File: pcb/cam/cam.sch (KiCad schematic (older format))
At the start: 93 parts, among them J1 Power In, J2 CONN_PRG_ESP, J3 CONN_PRG_STM, J4 Conn_01x26_Male, J5 SIM_Card, J6 Conn_Coaxial, Q1 IRLML6401, Q2 IRLML6401, U1 ESP32-WROOM-32U, U10 SRV05-4, U11 SIM800C, U2 TPS7A24, U3 FDC610, U4 XC6206-12, U5 XC6206-28, U6 MP2307, U7 MP2307, U8 STM8L051F3P, U9 LY68L6400, Y1 LSE

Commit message: Deleted old pcb; renamed discrete esp-s2 pcb to pcb
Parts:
- removed C22: 1u, Capacitor_SMD:C_0805_2012Metric, symbol Device:C_Small
- removed C24: 22u, 10V, Capacitor_SMD:C_1206_3216Metric, symbol Device:C_Small
- removed C26, C27: 470u, 10V, symbol Device:CP1_Small
- removed C30: 20p, Capacitor_SMD:C_0603_1608Metric, symbol Device:C_Small
- removed C6: 2.2uF, Capacitor_SMD:C_0805_2012Metric, symbol Device:C_Small
- removed J2: CONN_PRG_ESP, symbol Connector:Conn_01x03_Male
- removed J3: CONN_PRG_STM, symbol Connector:Conn_01x04_Male
- removed JP1: JMP_PGRM, symbol Jumper:Jumper_2_Open
- removed Q2: IRLML6401, Package_TO_SOT_SMD:SOT-23, symbol elktown-labs:IRLML6402
- removed R10: 6.8k, Resistor_SMD:R_0603_1608Metric, symbol Device:R_Small_US
- removed R12: 10k, 1%, Resistor_SMD:R_0603_1608Metric, symbol Device:R_Small_US
- removed R16: 100, Resistor_SMD:R_0603_1608Metric, symbol Device:R_Small_US
- removed R17: 10k, Resistor_SMD:R_0603_1608Metric, symbol Device:R_Small_US
- removed R18: 35.7k 1%, Resistor_SMD:R_0603_1608Metric, symbol Device:R_Small_US
- removed TP1: TestPoint, TestPoint:TestPoint_THTPad_1.5x1.5mm_Drill0.7mm, symbol Connector:TestPoint
- removed U1: ESP32-WROOM-32U, RF_Module:ESP32-WROOM-32U, symbol RF_Module:ESP32-WROOM-32U
- removed U2: TPS7A24, Package_TO_SOT_SMD:SOT-23-5, symbol elktown-labs:TPS7A24
- removed U6: MP2307, Package_SO:SOIC-8-1EP_3.9x4.9mm_P1.27mm_EP2.514x3.2mm, symbol elktown-labs:MP2307
- removed U8: STM8L051F3P, Package_SO:TSSOP-20_4.4x6.5mm_P0.65mm, symbol MCU_ST_STM8:STM8L051F3P
- added C10, C7: TBD, Capacitor_SMD:C_0603_1608Metric, symbol Device:C_Small
- added C14, C4: 1u, Capacitor_SMD:C_0603_1608Metric, symbol Device:C_Small
- added C25, C26, C33, C34, C37, C39, C40, C41: 100n, Capacitor_SMD:C_0603_1608Metric, symbol Device:C_Small
- added C44: 100n, Capacitor_SMD:C_0603_1608Metric, symbol Device:CP1_Small
- added C48: 10u, Capacitor_SMD:C_0805_2012Metric, symbol Device:C_Small
- added C49: 33p, Capacitor_SMD:C_0603_1608Metric, symbol Device:C_Small
- added C5: 10u, 25V ceramic, Capacitor_SMD:C_1210_3225Metric, symbol Device:C_Small
- added C50: 10p, Capacitor_SMD:C_0603_1608Metric, symbol Device:C_Small
- added J1: Conn_Coaxial, Connector_Coaxial:U.FL_Hirose_U.FL-R-SMT-1_Vertical, symbol Connector:Conn_Coaxial
- added J3: PRGR, Connector_PinHeader_1.27mm:PinHeader_2x03_P1.27mm_Vertical, symbol Connector_Generic:Conn_02x03_Odd_Even
- added J7: JTAG, Connector_PinHeader_1.27mm:PinHeader_2x05_P1.27mm_Vertical, symbol Connector_Generic:Conn_02x05_Odd_Even
- added L1: open, Inductor_SMD:L_0603_1608Metric, symbol Device:L_Small
- added R28: 0, Resistor_SMD:R_0603_1608Metric, symbol Device:R_Small_US
- added R29, R32, R9: 10k, Resistor_SMD:R_0603_1608Metric, symbol Device:R_Small_US
- added R3: open, Resistor_SMD:R_0603_1608Metric, symbol Device:R_Small_US
- added R30, R31: 4.7k, Resistor_SMD:R_0603_1608Metric, symbol Device:R_Small_US
- added R4: 50mOhm 1%, Inductor_SMD:L_1206_3216Metric, symbol Device:R_Small_US
- added R7: 1M, Resistor_SMD:R_0603_1608Metric, symbol Device:R_Small_US
- added U1: TPS22810, Package_TO_SOT_SMD:SOT-23-6, symbol elktown-labs:TPS22810
- added U10: W25Q128JVS, Package_SO:SOIC-8_5.23x5.23mm_P1.27mm, symbol Memory_Flash:W25Q128JVS
- added U5: LTC3103, Package_SO:MSOP-10-1EP_3x3mm_P0.5mm_EP1.68x1.88mm, symbol elktown-labs:LTC3103
- added U6: INA226, Package_SO:VSSOP-10_3x3mm_P0.5mm, symbol Analog_ADC:INA226
- added U7: ESP32-S2, Package_DFN_QFN:QFN-56-1EP_7x7mm_P0.4mm_EP5.6x5.6mm_ThermalVias, symbol elktown-labs:ESP32-S2
- added Y2: 40Mhz, Crystal:Crystal_SMD_5032-4Pin_5.0x3.2mm, symbol Device:Crystal_GND24_Small
- C1: value 10n -> open
- C11: value 10u, 25V, CERAMIC -> 1u, 25V CERAMIC; footprint Capacitor_SMD:C_1210_3225Metric -> Capacitor_SMD:C_0805_2012Metric
- C12: value 10u, 25V -> TBD; footprint Capacitor_SMD:C_1210_3225Metric -> Capacitor_SMD:C_0603_1608Metric
- C13: value 100n -> TBD
- C15: value 3.9n -> 1u
- C18: renamed from C17; value 10nF -> 22n
- C19: value 22u, 10V -> 22p; footprint Capacitor_SMD:C_1206_3216Metric -> Capacitor_SMD:C_0603_1608Metric
- C2: value 1u -> short; footprint Capacitor_SMD:C_0805_2012Metric -> Capacitor_SMD:C_0603_1608Metric
- C20: value 22u, 10V -> 100n; footprint Capacitor_SMD:C_1206_3216Metric -> Capacitor_SMD:C_0603_1608Metric
- C21: value 10n -> 47u; footprint Capacitor_SMD:C_0603_1608Metric -> Capacitor_SMD:C_1206_3216Metric
- C22: renamed from C10; value 10u, 25V -> 22u, 25V
- C29: value 20p -> 10u; footprint Capacitor_SMD:C_0603_1608Metric -> Capacitor_SMD:C_0805_2012Metric
- C3: value 1u -> 100p; footprint Capacitor_SMD:C_0805_2012Metric -> Capacitor_SMD:C_0603_1608Metric
- C32: renamed from C18; value 10nF -> 10n
- C38: renamed from C25; value 22u, 10V -> 100u, 10V
- C6: renamed from C9; value 10u, 25V, CERAMIC -> 100n; footprint Capacitor_SMD:C_1210_3225Metric -> Capacitor_SMD:C_0603_1608Metric
- D2: renamed from D3; symbol Device:LED -> Device:LED_Small
- D3: renamed from D2; symbol Device:LED -> Device:LED_Small
- J2: renamed from J1; footprint (none) -> Connector_JST:JST_XH_B2B-XH-A_1x02_P2.50mm_Vertical
- J4: value Conn_01x26_Male -> Conn_01x24_Male; footprint (none) -> Connector_FFC-FPC:Hirose_FH12-24S-0.5SH_1x24-1MP_P0.50mm_Horizontal; symbol Connector:Conn_01x26_Male -> Connector:Conn_01x24_Male
- L2: renamed from L1; footprint (none) -> Elktown Footprints:IND_LPS3314-222MRC
- L3: renamed from L2; value 10u, 3A -> 15u, 2.3A; footprint (none) -> Elktown Footprints:MSS7348-XXXMEC; Model (none) -> CDRH127/LD
- Q1: value IRLML6401 -> IRLML6402
- R1: value 10k -> 0
- R10: renamed from R9; value 10k -> 47k
- R11: renamed from R7; value 1k -> 4.7k
- R14: value 26.1k, 1% -> 4.7k
- R15: renamed from R13; value 10k, 1% -> 10k
- R16: renamed from R15; value 33.2k, 1% -> 33.2k
- R18: renamed from R4; value 1k -> TBD
- R19: value 10k 1% -> TBD
- R2: value 100 -> 10k
- R5: value 1k -> 0; footprint Resistor_SMD:R_0603_1608Metric -> Inductor_SMD:L_0603_1608Metric
- R6: value 1k -> 442k
- R8: value 10k -> 2M
- TP1: renamed from TP2; value TestPoint -> 1V2; footprint TestPoint:TestPoint_THTPad_1.5x1.5mm_Drill0.7mm -> TestPoint:TestPoint_Loop_D2.60mm_Drill0.9mm_Beaded
- TP2: renamed from TP3; value TestPoint -> 2V8; footprint TestPoint:TestPoint_THTPad_1.5x1.5mm_Drill0.7mm -> TestPoint:TestPoint_Loop_D2.60mm_Drill0.9mm_Beaded
- TP3: renamed from TP4; value TestPoint -> 3V3; footprint TestPoint:TestPoint_THTPad_1.5x1.5mm_Drill0.7mm -> TestPoint:TestPoint_Loop_D2.60mm_Drill0.9mm_Beaded
- TP4: renamed from TP5; value TestPoint -> 4V; footprint TestPoint:TestPoint_THTPad_1.5x1.5mm_Drill0.7mm -> TestPoint:TestPoint_Loop_D2.60mm_Drill0.9mm_Beaded
- U2: renamed from U3; footprint Package_SO:TSSOP-8_3x3mm_P0.65mm -> Package_TO_SOT_SMD:SuperSOT-6
- Y1: value LSE -> 32.768kHz; footprint (none) -> Crystal:Crystal_SMD_SeikoEpson_MC306-4Pin_8.0x3.2mm
- renumbered C7 to C16, C8 to C17, C14 to C27, C16 to C30, C31 to C42, C32 to C43, C34 to C45, C33 to C46, C4 to C8, C5 to C9, R11 to R12, R3 to R13, R20 to R17, R21 to R20, R22 to R21, R23 to R22, R24 to R23, R25 to R24, R26 to R25, R27 to R26, R28 to R27, U9 to U11, U10 to U12, U11 to U13, U4 to U3, U5 to U4, U7 to U8
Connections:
- net labels added: PRGRM, SCL_AUX, SCL_CAM, SDA_AUX, SDA_CAM, SD_DATA0, SD_DATA1, SD_DATA2, SD_DATA3, SPICLK, SPICS0, SPICS1, TCK, TDI, TDO, TMS, VDD_SDIO, XTAL32N, XTAL32P, XTALN, XTALP, ~RST
- net labels removed: ESP32_EN, MASTER_EN, PSRAM_CE, PSRAM_SCLK, PSRAM_SI, PSRAM_SIO2, PSRAM_SIO3, PSRAM_SO, SCL, SDA, STDBY_3V3, STM8_NRST, SWIM, VSUPPLY_MEASURE, VSUPPLY_MEASURE_EN
- wire segments 418 -> 541
- no-connect marks 36 -> 30
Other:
- moved on the sheet: C18, C22, C38, C45, C46, C6, D1, J2, L2, R11, R13, R17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

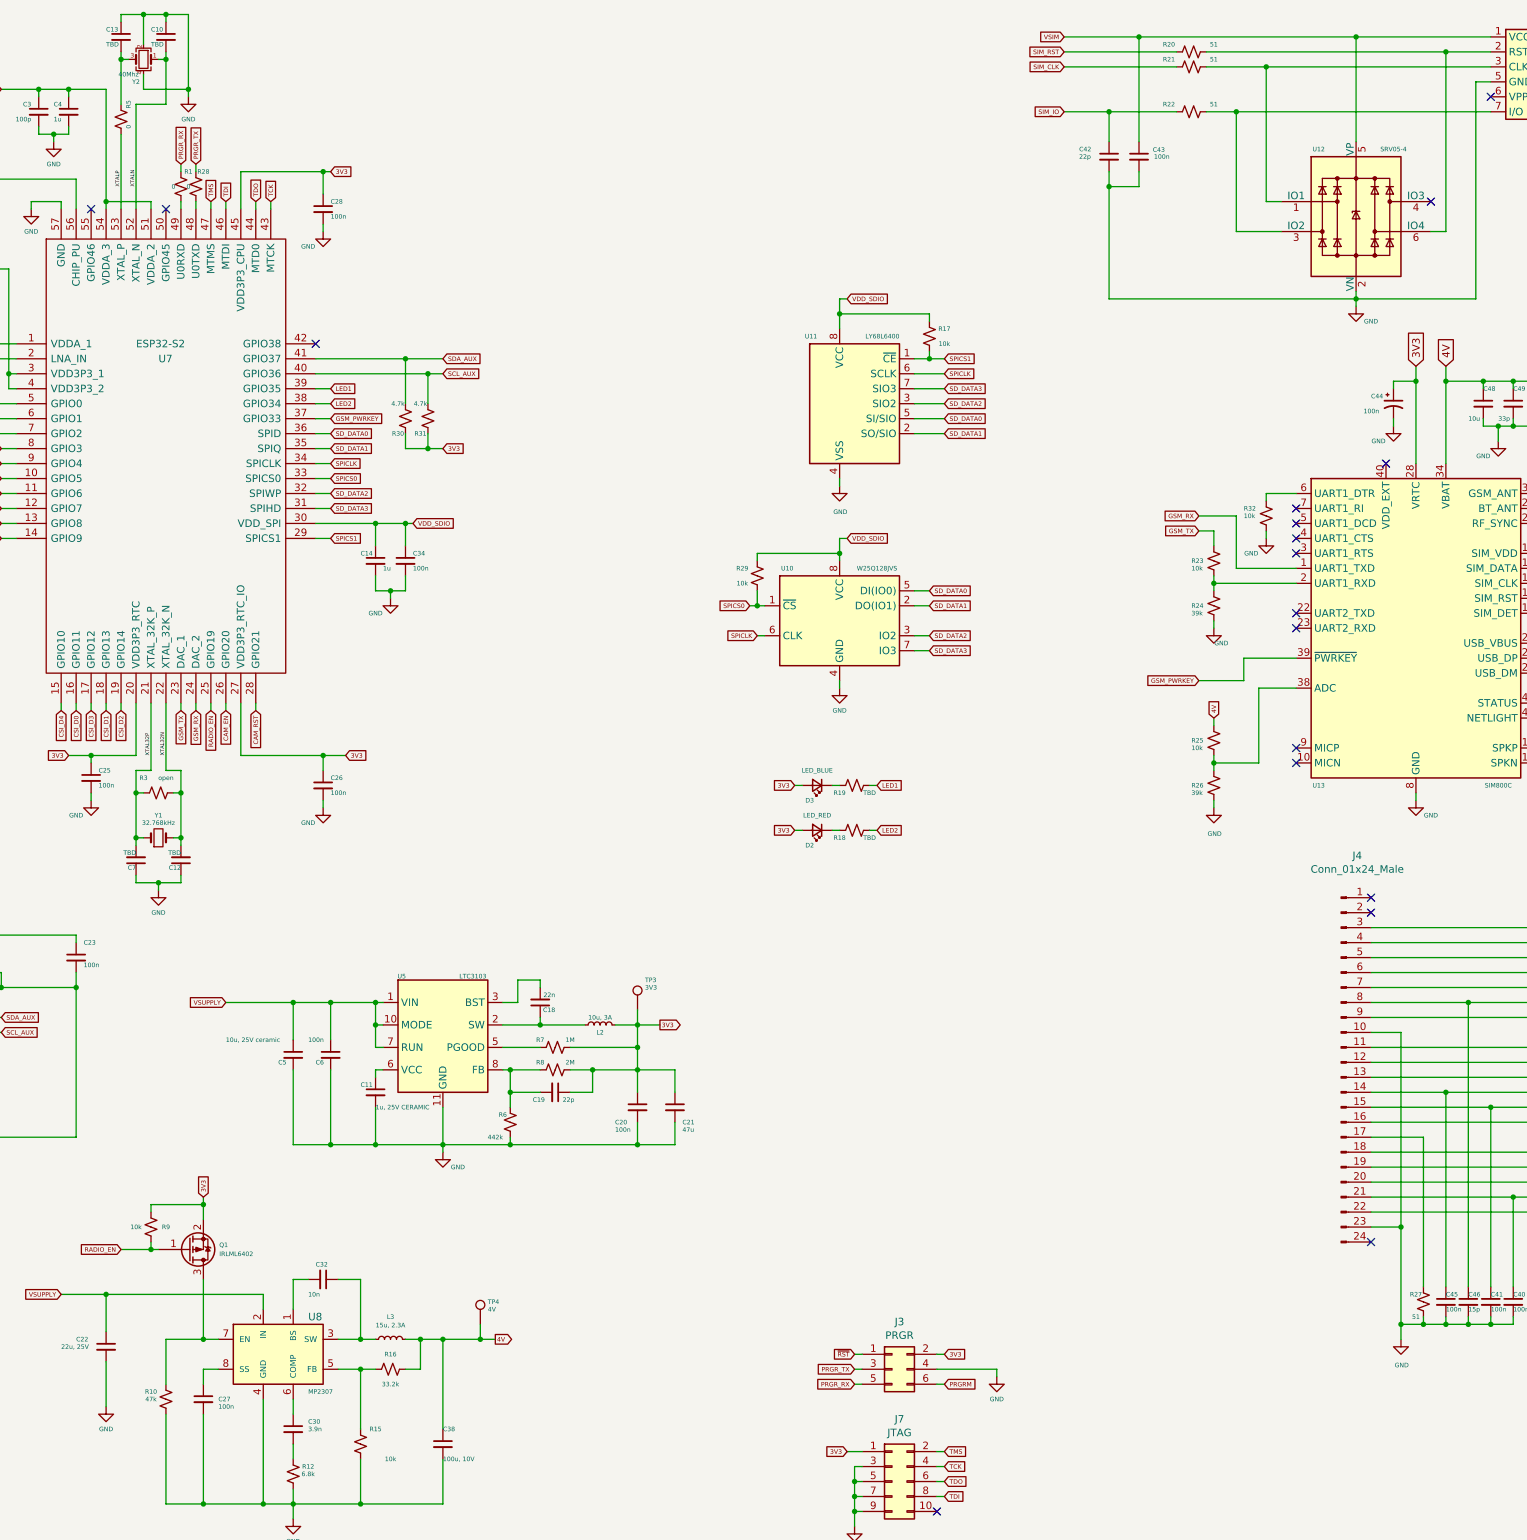
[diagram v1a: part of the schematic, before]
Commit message: PCB: Updated values of some components
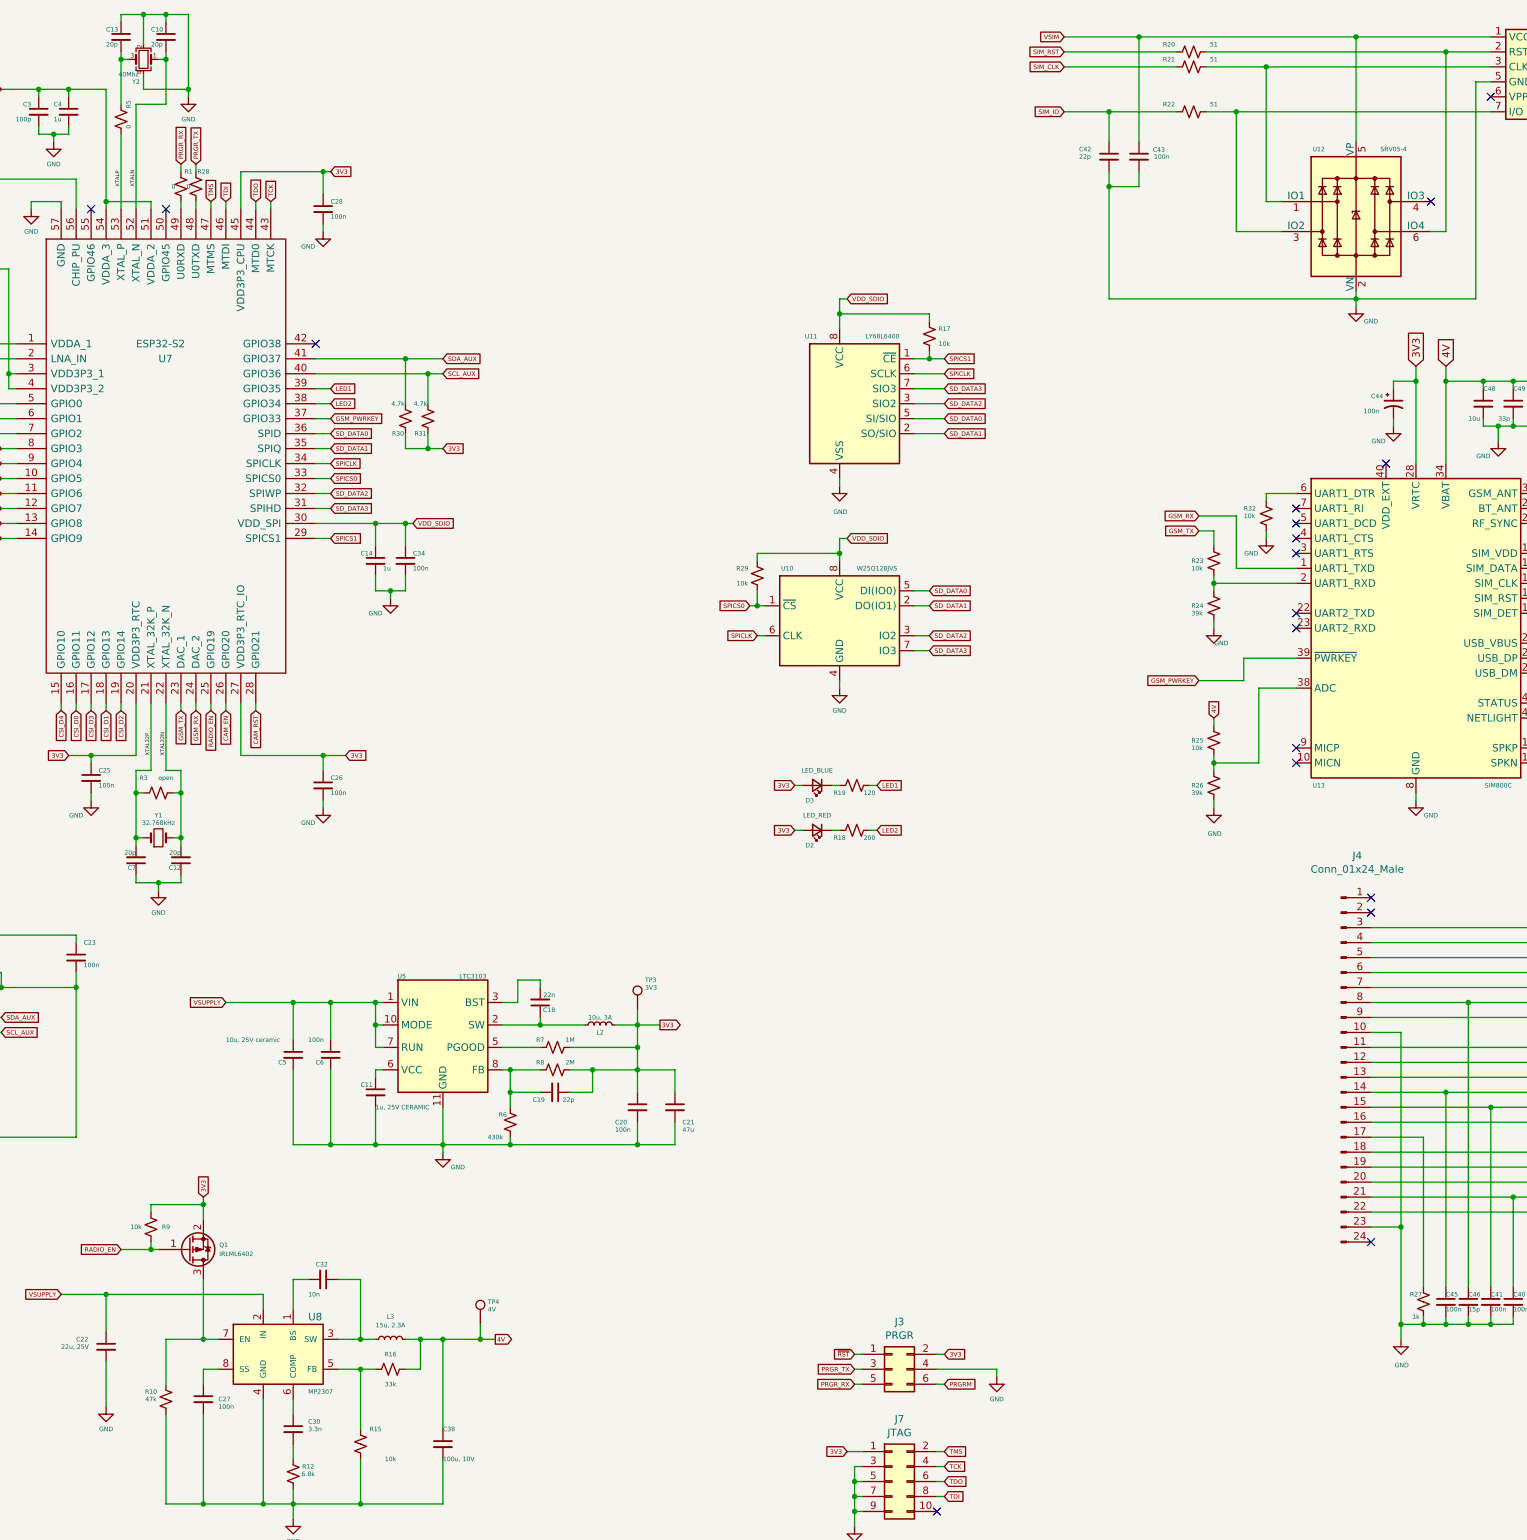
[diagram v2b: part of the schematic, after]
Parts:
- C10, C12, C13, C7: value TBD -> 20p
- C30: value 3.9n -> 3.3n
- R16: value 33.2k -> 33k
- R18: value TBD -> 200
- R19: value TBD -> 120
- R27: value 51 -> 1k
- R6: value 442k -> 430k
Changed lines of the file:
@@
 P 14000 9250
 F 0 "R27" H 14050 9200 30  0000 C CNN
-F 1 "51" H 14050 9350 30  0000 C CNN
+F 1 "1k" H 14050 9350 30  0000 C CNN
 F 2 "Resistor_SMD:R_0603_1608Metric" H 14000 9250 50  0001 C CNN
 F 3 "~" H 14000 9250 50  0001 C CNN
@@
 P 7900 8050
 F 0 "R6" H 7950 8000 30  0000 C CNN
-F 1 "442k" H 8000 8150 30  0000 C CNN
+F 1 "430k" H 8000 8150 30  0000 C CNN
 F 2 "Resistor_SMD:R_0603_1608Metric" H 7900 8050 50  0001 C CNN
 F 3 "~" H 7900 8050 50  0001 C CNN
@@
 P 5600 800
 F 0 "C10" H 5500 850 30  0000 L CNN
-F 1 "TBD" H 5500 750 30  0000 L CNN
+F 1 "20p" H 5500 750 30  0000 L CNN
 F 2 "Capacitor_SMD:C_0603_1608Metric" H 5600 800 50  0001 C CNN
 F 3 "~" H 5600 800 50  0001 C CNN
@@
 P 5300 800
 F 0 "C13" H 5200 850 30  0000 L CNN
-F 1 "TBD" H 5200 750 30  0000 L CNN
+F 1 "20p" H 5200 750 30  0000 L CNN
 F 2 "Capacitor_SMD:C_0603_1608Metric" H 5300 800 50  0001 C CNN
 F 3 "~" H 5300 800 50  0001 C CNN
@@
 Wire Wire Line
 	5200 9450 5200 9200
-$Comp
-L Device:C_Small C22
-U 1 1 5EBF5251
-P 5200 9550
-F 0 "C22" H 5000 9600 30  0000 L CNN
-F 1 "22u, 25V" H 4900 9550 30  0000 L CNN
-F 2 "Capacitor_SMD:C_1210_3225Metric" H 5200 9550 50  0001 C CNN
-F 3 "~" H 5200 9550 50  0001 C CNN
-	1    5200 9550
-	1    0    0    -1
-$EndComp
 Text GLabel 4900 9200 0    30   Input ~ 0
 VSUPPLY
@@
 P 7100 9700
 F 0 "R16" V 7200 9700 30  0000 C CNN
-F 1 "33.2k" V 7000 9700 30  0000 C CNN
+F 1 "33k" V 7000 9700 30  0000 C CNN
 F 2 "Resistor_SMD:R_0603_1608Metric" H 7100 9700 50  0001 C CNN
 F 3 "~" H 7100 9700 50  0001 C CNN
@@
 P 6450 10100
 F 0 "C30" H 6550 10150 30  0000 L CNN
-F 1 "3.9n" H 6550 10100 30  0000 L CNN
+F 1 "3.3n" H 6550 10100 30  0000 L CNN
 F 2 "Capacitor_SMD:C_0603_1608Metric" H 6450 10100 50  0001 C CNN
 F 3 "~" H 6450 10100 50  0001 C CNN
@@
 P 10200 5800
 F 0 "R19" V 10250 5700 30  0000 C CNN
-F 1 "TBD" V 10250 5900 30  0000 C CNN
+F 1 "120" V 10250 5900 30  0000 C CNN
 F 2 "Resistor_SMD:R_0603_1608Metric" H 10200 5800 50  0001 C CNN
 F 3 "~" H 10200 5800 50  0001 C CNN
@@
 P 10200 6100
 F 0 "R18" V 10250 6000 30  0000 C CNN
-F 1 "TBD" V 10250 6200 30  0000 C CNN
+F 1 "200" V 10250 6200 30  0000 C CNN
 F 2 "Resistor_SMD:R_0603_1608Metric" H 10200 6100 50  0001 C CNN
 F 3 "~" H 10200 6100 50  0001 C CNN
@@
 P 5400 6300
 F 0 "C7" H 5400 6350 30  0000 L CNN
-F 1 "TBD" H 5400 6250 30  0000 L CNN
+F 1 "20p" H 5400 6250 30  0000 L CNN
 F 2 "Capacitor_SMD:C_0603_1608Metric" H 5400 6300 50  0001 C CNN
 F 3 "~" H 5400 6300 50  0001 C CNN
@@
 P 5700 6300
 F 0 "C12" H 5700 6350 30  0000 L CNN
-F 1 "TBD" H 5700 6250 30  0000 L CNN
+F 1 "20p" H 5700 6250 30  0000 L CNN
 F 2 "Capacitor_SMD:C_0603_1608Metric" H 5700 6300 50  0001 C CNN
 F 3 "~" H 5700 6300 50  0001 C CNN
@@
 Text GLabel 10700 4600 2    30   Input ~ 0
 SD_DATA1
+$Comp
+L Device:C_Small C22
+U 1 1 5EBF5251
+P 5200 9550
+F 0 "C22" H 5000 9600 30  0000 L CNN
+F 1 "22u, 25V" H 4900 9550 30  0000 L CNN
+F 2 "Capacitor_SMD:C_1210_3225Metric" H 5200 9550 50  0001 C CNN
+F 3 "~" H 5200 9550 50  0001 C CNN
+	1    5200 9550
+	1    0    0    -1
+$EndComp
 $EndSCHEMATC
